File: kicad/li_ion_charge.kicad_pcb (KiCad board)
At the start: 2 copper layers, 18 parts, among them P101 USB_B, P102 CONN_01X02, P103 CONN_01X02, U101 MCP73834-FCI/UN

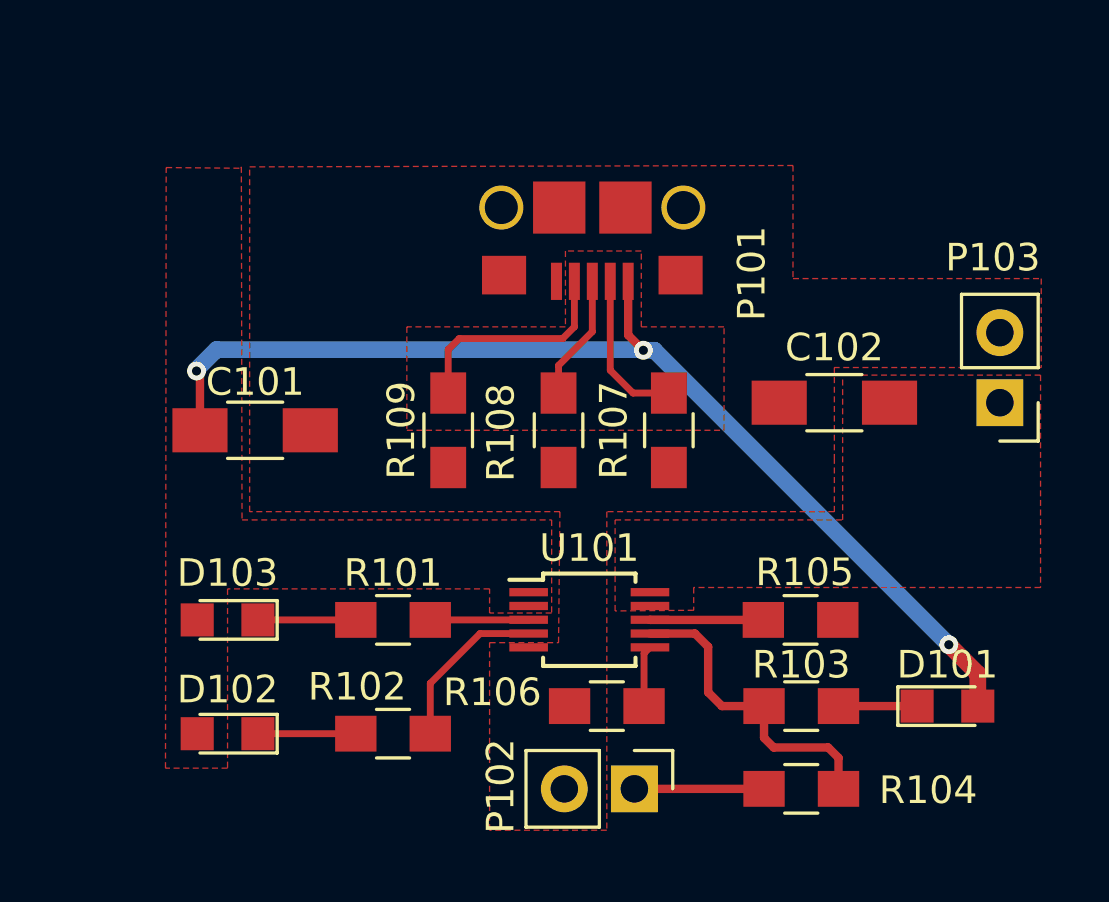
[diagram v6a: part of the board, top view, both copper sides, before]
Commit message: add power planes to back side
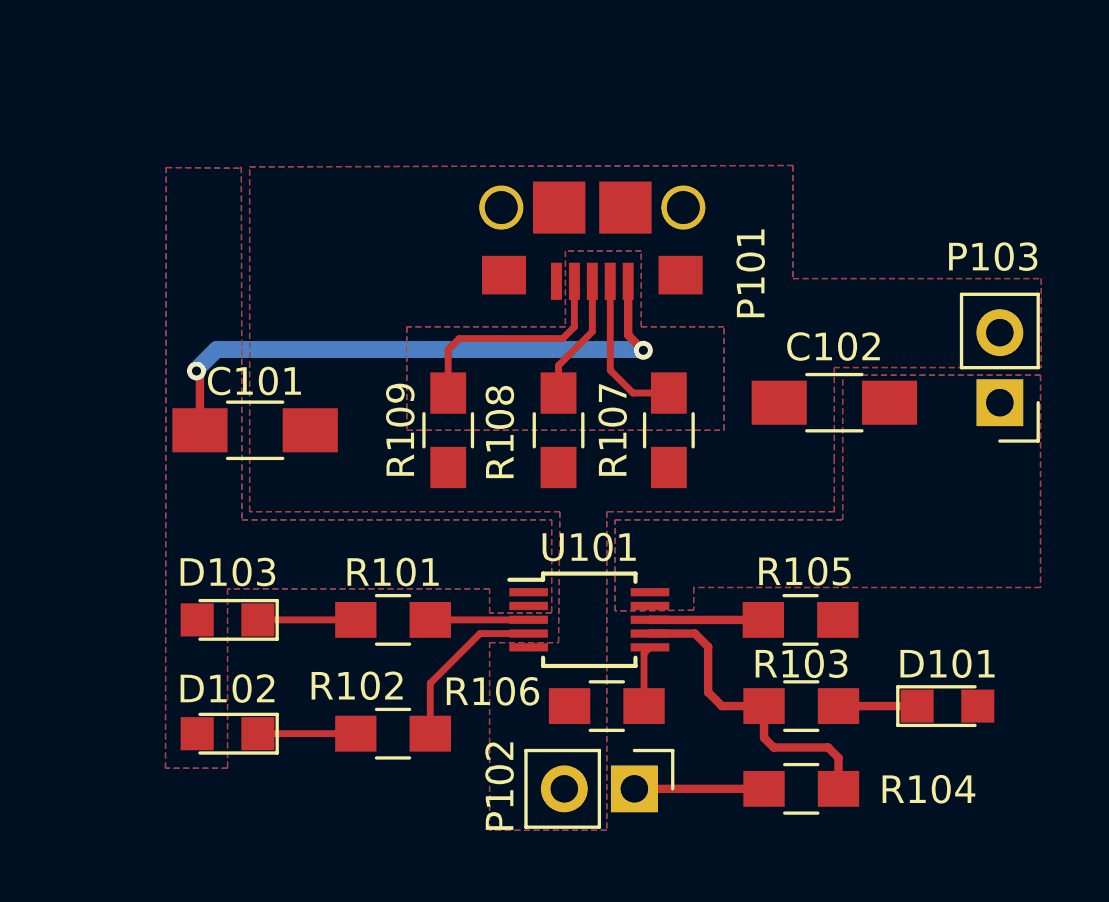
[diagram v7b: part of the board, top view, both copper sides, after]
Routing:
- net /VIN: track 39.6 -> 21.5 mm, vias 3 -> 2
- added copper zone on B.Cu, net /VBAT
- added copper zone on B.Cu, net /VIN
- added copper zone on B.Cu, net GND
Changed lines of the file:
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@@
   (general
     (links 38)
-    (no_connects 1)
-    (area 85.960599 43.671299 184.429 114.087333)
+    (no_connects 2)
+    (area 86.062199 43.772899 177.985734 113.985733)
     (thickness 1.6)
     (drawings 0)
-    (tracks 51)
+    (tracks 46)
     (zones 0)
     (modules 18)
@@
   )
   (setup
-    (last_trace_width 0.6096)
+    (last_trace_width 0.1524)
     (user_trace_width 0.3048)
     (user_trace_width 0.6096)
     (trace_clearance 0.1524)
-    (zone_clearance 0)
+    (zone_clearance 0.1524)
     (zone_45_only no)
     (trace_min 0.1524)
@@
   (segment (start 159.7 94.65) (end 161 94.65) (width 0.25) (layer F.Cu) (net 6))
   (segment (start 158.875 93.825) (end 159.7 94.65) (width 0.25) (layer F.Cu) (net 6))
-  (segment (start 172.2 106) (end 172.2 104.825) (width 0.6096) (layer F.Cu) (net 8))
-  (segment (start 160.475 93.1) (end 160.075 93.1) (width 0.6096) (layer B.Cu) (net 8))
-  (segment (start 171.15 103.775) (end 160.475 93.1) (width 0.6096) (layer B.Cu) (net 8))
-  (via (at 171.15 103.775) (size 0.6858) (drill 0.3302) (layers F.Cu B.Cu) (net 8))
-  (segment (start 172.2 104.825) (end 171.15 103.775) (width 0.6096) (layer F.Cu) (net 8))
   (segment (start 159.525 90.6) (end 159.525 92.55) (width 0.3048) (layer F.Cu) (net 8))
   (segment (start 144 93.975) (end 144 96) (width 0.3048) (layer F.Cu) (net 8))
@@
   )
   (zone (net 8) (net_name /VIN) (layer F.Cu) (hatch edge 0.508)
-    (connect_pads yes (clearance 0))
+    (connect_pads yes (clearance 0.1524))
     (min_thickness 0.254)
     (fill yes (arc_segments 16) (thermal_gap 0) (thermal_bridge_width 0.508))
@@
     (polygon
       (pts
+        (xy 174.475 101.7) (xy 161.9 101.7) (xy 161.9 102.525) (xy 159.05 102.55) (xy 159.05 99.25)
+        (xy 167.3 99.25) (xy 167.3 94) (xy 174.475 94)
+      )
+    )
+  )
+  (zone (net 8) (net_name /VIN) (layer B.Cu) (hatch edge 0.508)
+    (connect_pads yes (clearance 0.1524))
+    (min_thickness 0.254)
+    (fill (arc_segments 16) (thermal_gap 0) (thermal_bridge_width 0.508))
+    (polygon
+      (pts
+        (xy 145.5 86.45) (xy 145.525 99.25) (xy 156.75 99.25) (xy 156.75 102.625) (xy 154.5 102.625)
+        (xy 154.5 101.75) (xy 145 101.75) (xy 145 108.25) (xy 142.75 108.25) (xy 142.775 86.475)
+        (xy 145.5 86.5)
+      )
+    )
+  )
+  (zone (net 1) (net_name GND) (layer B.Cu) (hatch edge 0.508)
+    (connect_pads (clearance 0.1524))
+    (min_thickness 0.254)
+    (fill (arc_segments 16) (thermal_gap 0.1524) (thermal_bridge_width 0.508))
+    (polygon
+      (pts
+        (xy 165.5 90.5) (xy 174.5 90.5) (xy 174.5 93.725) (xy 167 93.725) (xy 167 97)
+        (xy 167 98.95) (xy 158.75 98.95) (xy 158.75 105) (xy 158.75 110.5) (xy 154.5 110.5)
+        (xy 154.5 103.7) (xy 157 103.7) (xy 157.05 98.95) (xy 145.8 98.95) (xy 145.8 86.45)
+        (xy 165.5 86.4)
+      )
+    )
+    (polygon
+      (pts        (xy 157.25 89.5) (xy 157.25 92.25) (xy 151.5 92.25) (xy 151.5 96) (xy 163 96)
+        (xy 163 92.25) (xy 160 92.25) (xy 160 89.5)
+      )
+    )
+  )
+  (zone (net 7) (net_name /VBAT) (layer B.Cu) (hatch edge 0.508)
+    (connect_pads yes (clearance 0))
+    (min_thickness 0.254)
+    (fill (arc_segments 16) (thermal_gap 0) (thermal_bridge_width 0.508))
+    (polygon
+      (pts

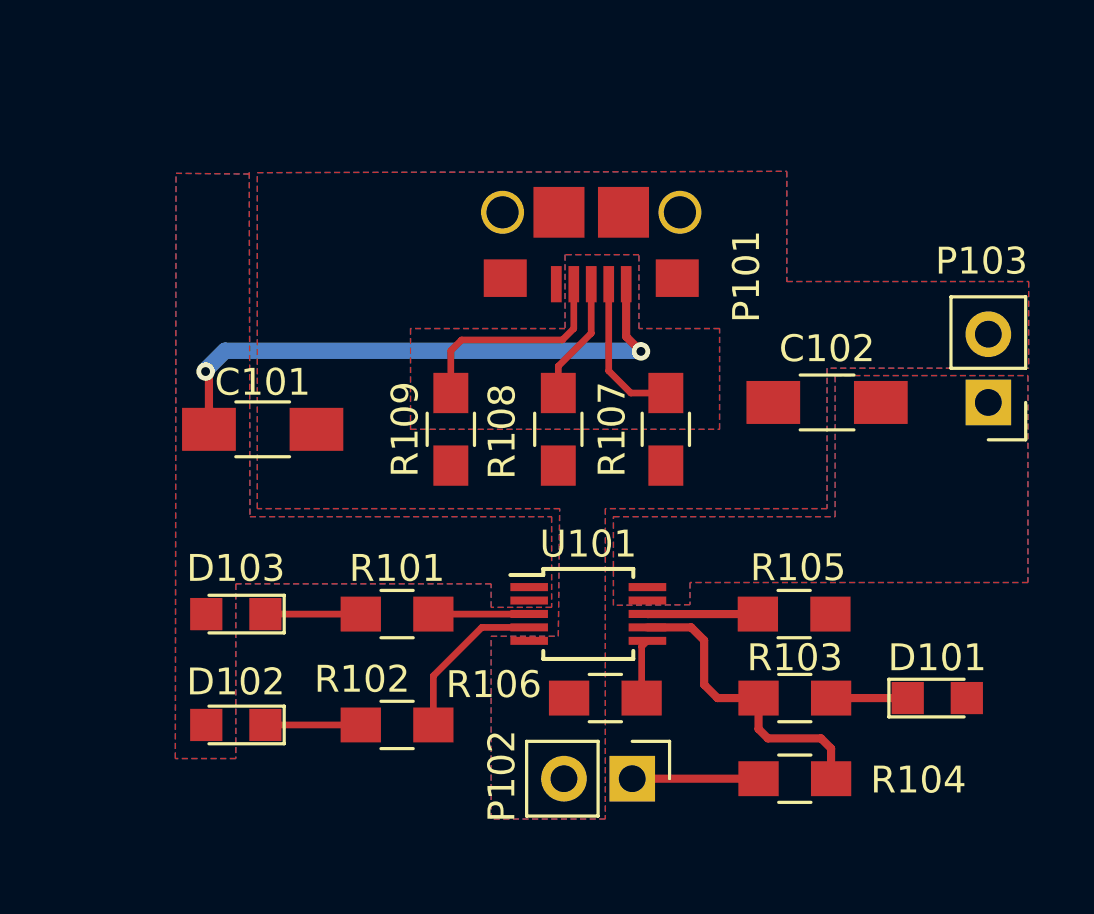
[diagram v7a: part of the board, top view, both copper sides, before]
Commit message: cleanup of zones, added zone for power from Vin pin, and initial edge cuts of board
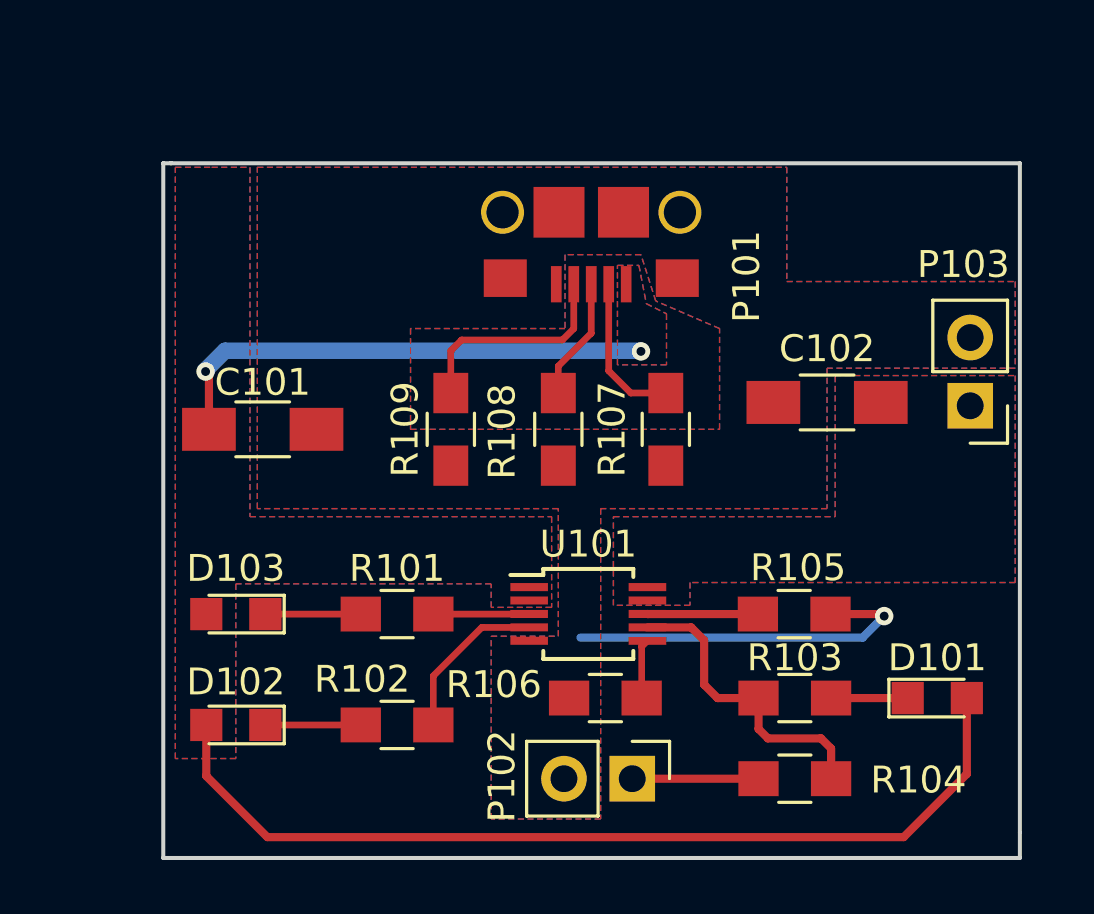
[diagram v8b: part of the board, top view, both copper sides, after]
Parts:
- moved P103 0.69 mm to (172.3, 95.1)
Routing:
- net /VIN: track 21.5 -> 53.7 mm
- net GND: track 0.00 -> 13.7 mm, vias 0 -> 1
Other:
- board outline added: 31.9 x 25.9 mm
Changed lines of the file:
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@@
   (general
     (links 38)
-    (no_connects 2)
+    (no_connects 0)
     (area 86.062199 43.772899 177.985734 113.985733)
     (thickness 1.6)
-    (drawings 0)
-    (tracks 46)
+    (drawings 6)
+    (tracks 54)
     (zones 0)
     (modules 18)
@@
   )
   (setup
-    (last_trace_width 0.1524)
+    (last_trace_width 0.3048)
     (user_trace_width 0.3048)
     (user_trace_width 0.6096)
@@
   )
   (module Pin_Headers:Pin_Header_Straight_1x02_Pitch2.54mm (layer F.Cu)
-    (at 173 95 180)
+    (at 172.325 95.125 180)
     (descr "Through hole straight pin header, 1x02, 2.54mm pitch, single row")
     (tags "Through hole pin header THT 1x02 2.54mm single row")
@@
     )
   )
+  (gr_line (start 142.3 86.1) (end 142.6 86.1) (angle 90) (layer Edge.Cuts) (width 0.15))
+  (gr_line (start 142.3 111.95) (end 142.3 86.1) (angle 90) (layer Edge.Cuts) (width 0.15))
+  (gr_line (start 174.175 111.95) (end 142.3 111.95) (angle 90) (layer Edge.Cuts) (width 0.15))
+  (gr_line (start 174.175 111) (end 174.175 111.95) (angle 90) (layer Edge.Cuts) (width 0.15))
+  (gr_line (start 174.175 86.1) (end 174.175 111) (angle 90) (layer Edge.Cuts) (width 0.15))
+  (gr_line (start 142.575 86.1) (end 174.175 86.1) (angle 90) (layer Edge.Cuts) (width 0.15))
   (segment (start 86.3396 44.0503) (end 86.3396 44.7396) (width 0.25) (layer F.Cu) (net 0))
   (segment (start 96.6 58.05) (end 96.4 58.25) (width 0.25) (layer F.Cu) (net 0))
+  (segment (start 167.125 102.875) (end 169.05 102.875) (width 0.3048) (layer F.Cu) (net 1))
+  (segment (start 168.325 103.75) (end 157.825 103.75) (width 0.3048) (layer B.Cu) (net 1))
+  (segment (start 169.125 102.95) (end 168.325 103.75) (width 0.3048) (layer B.Cu) (net 1))
+  (via (at 169.125 102.95) (size 0.6858) (drill 0.3302) (layers F.Cu B.Cu) (net 1))
+  (segment (start 169.05 102.875) (end 169.125 102.95) (width 0.3048) (layer F.Cu) (net 1))
   (segment (start 167.15 106) (end 170 106) (width 0.3048) (layer F.Cu) (net 2))
   (segment (start 146.1 107) (end 149.65 107) (width 0.25) (layer F.Cu) (net 3))
@@
   (segment (start 159.7 94.65) (end 161 94.65) (width 0.25) (layer F.Cu) (net 6))
   (segment (start 158.875 93.825) (end 159.7 94.65) (width 0.25) (layer F.Cu) (net 6))
-  (segment (start 159.525 90.6) (end 159.525 92.55) (width 0.3048) (layer F.Cu) (net 8))
   (segment (start 144 93.975) (end 144 96) (width 0.3048) (layer F.Cu) (net 8))
   (segment (start 143.875 93.85) (end 144 93.975) (width 0.3048) (layer F.Cu) (net 8))
@@
   (segment (start 160.075 93.1) (end 160.05 93.075) (width 0.3048) (layer B.Cu) (net 8))
   (via (at 160.075 93.1) (size 0.6858) (drill 0.3302) (layers F.Cu B.Cu) (net 8))
-  (segment (start 159.525 92.55) (end 160.075 93.1) (width 0.3048) (layer F.Cu) (net 8))
+  (segment (start 143.9 107) (end 143.9 108.9) (width 0.3048) (layer F.Cu) (net 8))
+  (segment (start 143.9 108.9) (end 146.175 111.175) (width 0.3048) (layer F.Cu) (net 8))
+  (segment (start 146.175 111.175) (end 169.85 111.175) (width 0.3048) (layer F.Cu) (net 8))
+  (segment (start 169.85 111.175) (end 172.2 108.825) (width 0.3048) (layer F.Cu) (net 8))
+  (segment (start 172.2 108.825) (end 172.2 106) (width 0.3048) (layer F.Cu) (net 8))
   (segment (start 164.45 109) (end 159.75 109) (width 0.3048) (layer F.Cu) (net 9))
   (segment (start 164.45 106) (end 162.925 106) (width 0.3048) (layer F.Cu) (net 10))
@@
     (polygon
       (pts
-        (xy 165.5 90.5) (xy 174.5 90.5) (xy 174.5 93.725) (xy 167 93.725) (xy 167 97)
-        (xy 167 98.95) (xy 158.75 98.95) (xy 158.75 105) (xy 158.75 110.5) (xy 154.5 110.5)
-        (xy 154.5 103.7) (xy 157 103.7) (xy 157.05 98.95) (xy 145.8 98.95) (xy 145.8 86.45)
-        (xy 165.5 86.4)
+        (xy 165.5 90.5) (xy 174 90.5) (xy 174 93.725) (xy 167 93.725) (xy 167 97)
+        (xy 167 98.95) (xy 158.575 98.95) (xy 158.575 104.975) (xy 158.575 110.5) (xy 154.5 110.5)
+        (xy 154.5 103.7) (xy 157 103.7) (xy 157 98.95) (xy 145.8 98.95) (xy 145.8 86.25)
+        (xy 165.5 86.25)
       )
     )
     (polygon
       (pts        (xy 157.25 89.5) (xy 157.25 92.25) (xy 151.5 92.25) (xy 151.5 96) (xy 163 96)
-        (xy 163 92.25) (xy 160 92.25) (xy 160 89.5)
+        (xy 163 92.25) (xy 160.625 91.225) (xy 160.075 89.5)
       )
     )
@@
     (polygon
       (pts
-        (xy 145.5 86.45) (xy 145.525 99.25) (xy 156.75 99.25) (xy 156.75 102.625) (xy 154.5 102.625)
-        (xy 154.5 101.75) (xy 145 101.75) (xy 145 108.25) (xy 142.75 108.25) (xy 142.775 86.475)
-        (xy 145.5 86.5)
+        (xy 145.525 86.25) (xy 145.525 99.25) (xy 156.75 99.25) (xy 156.75 102.625) (xy 154.5 102.625)
+        (xy 154.5 101.75) (xy 145 101.75) (xy 145 108.25) (xy 142.75 108.25) (xy 142.75 86.25)
+        (xy 144.1 86.25)
       )
     )
@@
     (polygon
       (pts
-        (xy 174.475 101.7) (xy 161.9 101.7) (xy 161.9 102.525) (xy 159.05 102.55) (xy 159.05 99.25)
-        (xy 167.3 99.25) (xy 167.3 94) (xy 174.475 94)
+        (xy 174 101.7) (xy 161.9 101.7) (xy 161.9 102.55) (xy 159.05 102.55) (xy 159.05 99.25)
+        (xy 167.3 99.25) (xy 167.3 94) (xy 174 94)
       )
     )
@@
     (connect_pads yes (clearance 0.1524))
     (min_thickness 0.254)
-    (fill (arc_segments 16) (thermal_gap 0) (thermal_bridge_width 0.508))
+    (fill yes (arc_segments 16) (thermal_gap 0) (thermal_bridge_width 0.508))
     (polygon
       (pts
-        (xy 145.5 86.45) (xy 145.525 99.25) (xy 156.75 99.25) (xy 156.75 102.625) (xy 154.5 102.625)
-        (xy 154.5 101.75) (xy 145 101.75) (xy 145 108.25) (xy 142.75 108.25) (xy 142.775 86.475)
-        (xy 145.5 86.5)
+        (xy 145.525 86.25) (xy 145.525 99.25) (xy 156.75 99.25) (xy 156.75 102.625) (xy 154.5 102.625)
+        (xy 154.5 101.75) (xy 145 101.75) (xy 145 108.25) (xy 142.75 108.25) (xy 142.75 86.25)
+        (xy 144.1 86.25)
+      )
+    )
+  )
+  (zone (net 7) (net_name /VBAT) (layer B.Cu) (hatch edge 0.508)
+    (connect_pads yes (clearance 0))
+    (min_thickness 0.254)
+    (fill yes (arc_segments 16) (thermal_gap 0) (thermal_bridge_width 0.508))
+    (polygon
+      (pts
+        (xy 174 101.7) (xy 161.9 101.7) (xy 161.9 102.55) (xy 159.05 102.55) (xy 159.05 99.25)
+        (xy 167.3 99.25) (xy 167.3 94) (xy 174 94)
       )
     )
@@
     (connect_pads (clearance 0.1524))
     (min_thickness 0.254)
-    (fill (arc_segments 16) (thermal_gap 0.1524) (thermal_bridge_width 0.508))
+    (fill yes (arc_segments 16) (thermal_gap 0.1524) (thermal_bridge_width 0.508))
     (polygon
       (pts
-        (xy 165.5 90.5) (xy 174.5 90.5) (xy 174.5 93.725) (xy 167 93.725) (xy 167 97)
-        (xy 167 98.95) (xy 158.75 98.95) (xy 158.75 105) (xy 158.75 110.5) (xy 154.5 110.5)
-        (xy 154.5 103.7) (xy 157 103.7) (xy 157.05 98.95) (xy 145.8 98.95) (xy 145.8 86.45)
-        (xy 165.5 86.4)
+        (xy 165.5 90.5) (xy 174 90.5) (xy 174 93.725) (xy 167 93.725) (xy 167 97)
+        (xy 167 98.95) (xy 158.575 98.95) (xy 158.575 104.975) (xy 158.575 110.5) (xy 154.5 110.5)
+        (xy 154.5 103.7) (xy 157 103.7) (xy 157 98.95) (xy 145.8 98.95) (xy 145.8 86.25)
+        (xy 165.5 86.25)
       )
     )
     (polygon
       (pts        (xy 157.25 89.5) (xy 157.25 92.25) (xy 151.5 92.25) (xy 151.5 96) (xy 163 96)
-        (xy 163 92.25) (xy 160 92.25) (xy 160 89.5)
+        (xy 163 92.25) (xy 160.625 91.225) (xy 160.075 89.5)
       )
     )
   )
-  (zone (net 7) (net_name /VBAT) (layer B.Cu) (hatch edge 0.508)
-    (connect_pads yes (clearance 0))
+  (zone (net 8) (net_name /VIN) (layer F.Cu) (hatch edge 0.508)
+    (connect_pads yes (clearance 0.1524))
     (min_thickness 0.254)
-    (fill (arc_segments 16) (thermal_gap 0) (thermal_bridge_width 0.508))
+    (fill yes (arc_segments 16) (thermal_gap 0.1524) (thermal_bridge_width 0.508))
     (polygon
       (pts
-        (xy 174.475 101.7) (xy 161.9 101.7) (xy 161.9 102.525) (xy 159.05 102.55) (xy 159.05 99.25)
-        (xy 167.3 99.25) (xy 167.3 94) (xy 174.475 94)
+        (xy 160.275 91.325) (xy 161.025 91.7) (xy 161.025 93.6) (xy 159.2 93.6) (xy 159.2 89.9)
+        (xy 160 89.9)
       )
     )
+  )
+  (zone (net 8) (net_name /VIN) (layer B.Cu) (hatch edge 0.508)
+    (connect_pads yes (clearance 0.1524))
+    (min_thickness 0.254)
+    (fill yes (arc_segments 16) (thermal_gap 0.1524) (thermal_bridge_width 0.508))
+    (polygon
+      (pts
+        (xy 160.275 91.325) (xy 161.025 91.7) (xy 161.025 93.6) (xy 159.2 93.6) (xy 159.2 89.9)
+        (xy 160 89.9)
+      )
+    )
